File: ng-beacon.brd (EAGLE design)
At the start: 71.1 x 76.2 mm, 7 parts

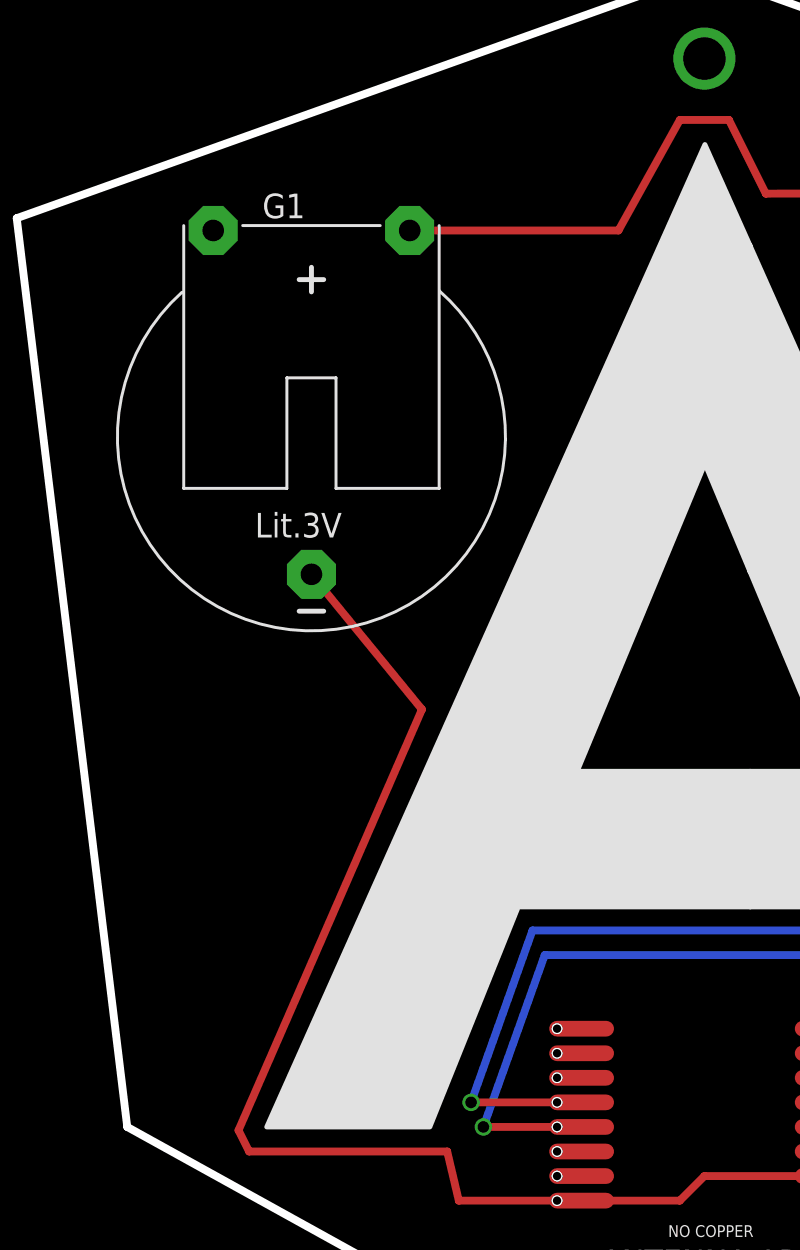
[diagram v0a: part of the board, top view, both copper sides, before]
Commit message: replace battery connector
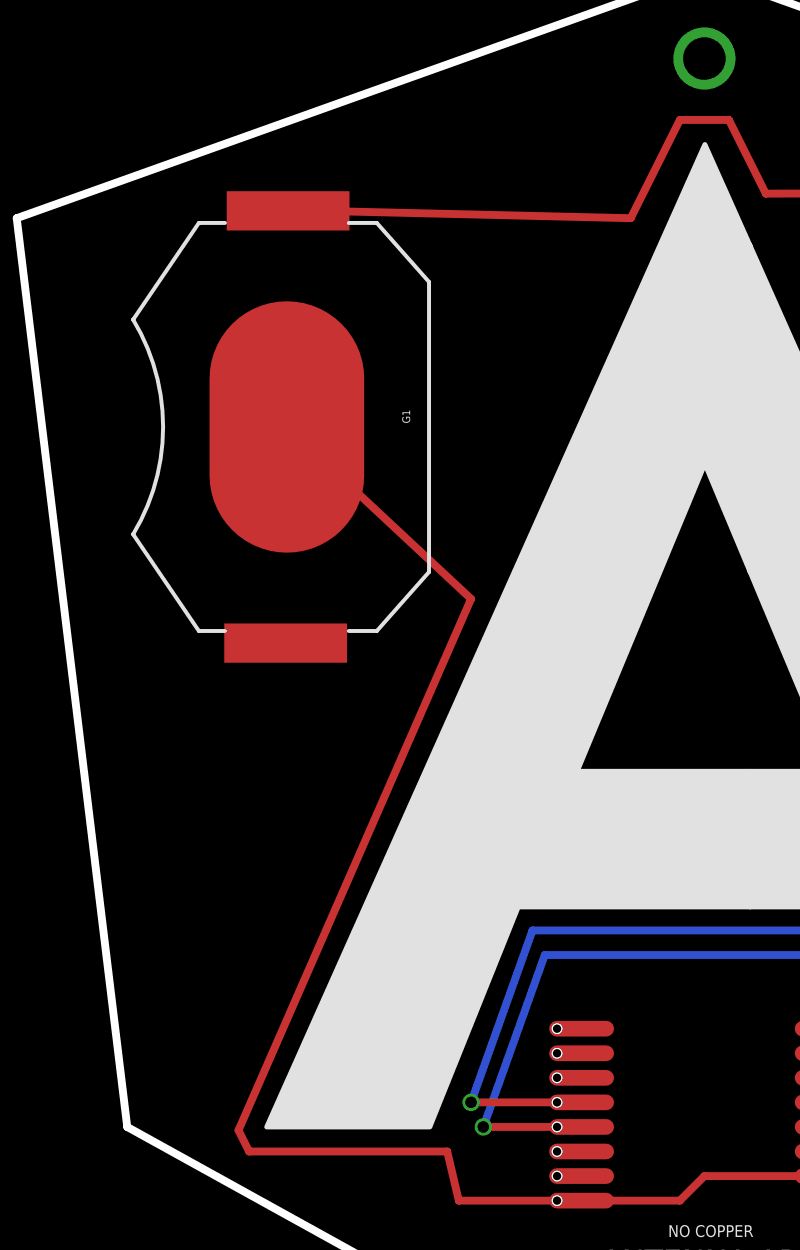
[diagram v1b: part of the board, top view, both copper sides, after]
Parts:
- G1: value CR2032H -> 20mm coincell; device battery:CR2032H -> SparkFun-Electromechanical:BATTCON_20MM_4LEGS
- moved G1 1.42 mm to (24.1, 51.4), turned to 270 degrees
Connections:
- net GND: now also G1.NEGATIVE; no longer G1.-
- net N$1: now also G1.POSITIVE@1, G1.POSITIVE@2, G1.POSITIVE@3, G1.POSITIVE@4; no longer G1.+
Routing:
- net GND: track 120.2 -> 130.4 mm
- net N$1: track 45.5 -> 50.0 mm
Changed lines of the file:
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@@
 </autorouter>
 <elements>
-<element name="G1" library="battery" package="CR2032H" value="CR2032H" x="25.4" y="50.8"/>
+<element name="G1" library="SparkFun-Electromechanical" package="BATTCON_20MM_4LEGS" value="20mm coincell" x="24.13" y="51.435" rot="R270">
+<attribute name="PROD_ID" value="BATT-10373" x="24.13" y="51.435" size="1.778" layer="27" rot="R270" display="off"/>
+<attribute name="VALUE" value="20mm coincell" x="24.13" y="51.435" size="1.778" layer="27" rot="R270" display="off"/>
+</element>
 <element name="U$1" library="PTR5518" package="PTR5518" value="PTR5518STD" x="45.72" y="13.97" rot="R180"/>
 <element name="S1" library="SparkFun-Electromechanical" package="AYZ0202" value="DPDT" x="71.630953125" y="60.047775" rot="R160">
@@
 </signal>
 <signal name="GND">
-<contactref element="G1" pad="-"/>
-<wire x1="25.4" y1="43.815" x2="31.115" y2="36.83" width="0.4064" layer="1"/>
-<wire x1="31.115" y1="36.83" x2="21.627896875" y2="15.06530625" width="0.4064" layer="1"/>
+<contactref element="G1" pad="NEGATIVE"/>
+<wire x1="24.13" y1="51.435" x2="33.655" y2="42.545" width="0.4064" layer="1"/>
+<wire x1="33.655" y1="42.545" x2="21.627896875" y2="15.06530625" width="0.4064" layer="1"/>
 <wire x1="21.627896875" y1="15.06530625" x2="22.17654375" y2="13.97" width="0.4064" layer="1"/>
 <wire x1="22.17654375" y1="13.97" x2="32.4203875" y2="13.97" width="0.4064" layer="1"/>
@@
 </signal>
 <signal name="N$1">
-<contactref element="G1" pad="+"/>
+<contactref element="G1" pad="POSITIVE@1"/>
 <contactref element="S1" pad="6"/>
-<wire x1="30.48" y1="61.595" x2="41.275" y2="61.595" width="0.4064" layer="1"/>
-<wire x1="41.275" y1="61.595" x2="44.45" y2="67.31" width="0.4064" layer="1"/>
+<wire x1="25.781" y1="62.611" x2="41.91" y2="62.23" width="0.4064" layer="1"/>
+<wire x1="41.91" y1="62.23" x2="44.45" y2="67.31" width="0.4064" layer="1"/>
 <wire x1="44.45" y1="67.31" x2="46.99" y2="67.31" width="0.4064" layer="1"/>
 <wire x1="46.99" y1="67.31" x2="48.895" y2="63.5" width="0.4064" layer="1"/>
 <wire x1="48.895" y1="63.5" x2="70.247928125" y2="63.55745625" width="0.4064" layer="1"/>
+<contactref element="G1" pad="POSITIVE@2"/>
+<contactref element="G1" pad="POSITIVE@3"/>
+<contactref element="G1" pad="POSITIVE@4"/>
 </signal>
 <signal name="VIN">

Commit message: remove temp sensor label
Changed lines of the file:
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@@
 <setting verticaltext="up"/>
 </settings>
-<grid distance="0.05" unitdist="inch" unit="inch" style="lines" multiple="1" display="no" altdistance="0.025" altunitdist="inch" altunit="inch"/>
+<grid distance="0.05" unitdist="inch" unit="mm" style="lines" multiple="1" display="no" altdistance="0.025" altunitdist="inch" altunit="inch"/>
 <layers>
 <layer number="1" name="Top" color="4" fill="1" visible="yes" active="yes"/>
@@
 <layer number="220" name="220bmp" color="21" fill="1" visible="no" active="no"/>
 <layer number="221" name="221bmp" color="22" fill="1" visible="no" active="no"/>
-<layer number="222" name="222bmp" color="23" fill="1" visible="no" active="no"/>
 <layer number="223" name="223bmp" color="24" fill="1" visible="no" active="no"/>
 <layer number="224" name="224bmp" color="25" fill="1" visible="no" active="no"/>
@@
 <attribute name="PROD_ID" value="CONN-09696" x="64.75070625" y="12.224234375" size="1.778" layer="27" rot="R209" display="off"/>
 </element>
-<element name="SN1" library="sensirion" package="DFN6/SHT" value="SHT21" x="66.04" y="35.56"/>
+<element name="SN1" library="sensirion" package="DFN6/SHT" value="SHT21" x="66.04" y="35.56" smashed="yes">
+<attribute name="VALUE" x="68.915" y="33.685" size="0.8128" layer="27" ratio="10" rot="R90"/>
+</element>
 <element name="R1" library="SparkFun-Resistors" package="0603-RES" value="10K" x="66.04" y="30.48">
 <attribute name="PROD_ID" value="RES-00824" x="66.04" y="30.48" size="1.778" layer="27" display="off"/>
@@
 <contactref element="G1" pad="POSITIVE@3"/>
 <contactref element="G1" pad="POSITIVE@4"/>
+<wire x1="22.606" y1="62.611" x2="25.781" y2="62.611" width="0" layer="19" extent="1-1"/>
+<wire x1="25.654" y1="40.259" x2="25.781" y2="62.611" width="0" layer="19" extent="1-1"/>
+<wire x1="22.479" y1="40.259" x2="25.654" y2="40.259" width="0" layer="19" extent="1-1"/>
 </signal>
 <signal name="VIN">
